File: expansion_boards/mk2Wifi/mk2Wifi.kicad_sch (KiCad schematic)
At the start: 23 parts, among them J0 TRIG_EXT, J2 USB_C_Receptacle_USB2.0_16P, J3 UART_EXT, J4 OLED, SW1 SW_Push, U1 ESP32-C3-MINI-1, U2 AP2112K-3.3

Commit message: Add mk2Wifi documentation, board images, and PCB/schematic updates
Add bilingual README (French default, English translation) with BOM,
connector pinouts, GPIO mapping, power supply details, programming
instructions, and USB-C safety warning. Include trimmed 3D render
images (front, back, SMD, bare board) in assets/ folder.

Co-Authored-By: Claude Opus 4.6 <noreply@anthropic.com>
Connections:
- net UART_RX: now also U1.31 (GPIO21/U0TXD); no longer U1.30 (GPIO20/U0RXD)
- net UART_TX: now also U1.30 (GPIO20/U0RXD); no longer U1.31 (GPIO21/U0TXD)
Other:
- company: (none) -> Mk2PVRouter.com
- title: (none) -> mk2Wifi
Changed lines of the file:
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@@
 	(generator_version "9.0")
 	(paper "A4")
+	(title_block
+		(title "mk2Wifi")
+		(date "2026-02-16")
+		(rev "v1.0")
+		(company "Mk2PVRouter.com")
+	)
 	(rectangle
 		(start 16.51 17.78)
@@
 		)
 	)
-	(text_box "See 4 Boot Configurations"
-		(exclude_from_sim no)
-		(at 25.4 45.72 0)
-		(size 27.94 3.81)
-		(margins 0.9525 0.9525 0.9525 0.9525)
-		(stroke
-			(width 0)
-			(type default)
-		)
-		(fill
-			(type none)
-		)
-		(effects
-			(font
-				(size 1.27 1.27)
-			)
-			(justify left top)
-		)
-	)
 	(junction
 		(at 26.67 102.87)
@@
 	)
 	(junction
+		(at 118.11 31.75)
+		(diameter 0)
+		(color 0 0 0 0)
+	)
+	(junction
 		(at 135.89 34.29)
 		(diameter 0)
@@
 	(wire
 		(pts
-			(xy 220.98 59.69) (xy 242.57 59.69)
+			(xy 220.98 59.69) (xy 241.3 59.69)
 		)
 		(stroke
@@
 	(wire
 		(pts
-			(xy 242.57 64.77) (xy 229.87 64.77)
+			(xy 241.3 64.77) (xy 229.87 64.77)
+		)
+		(stroke
+			(width 0)
+			(type default)
+		)
+	)
+	(wire
+		(pts
+			(xy 220.98 41.91) (xy 241.3 41.91)
 		)
 		(stroke
@@
 	(wire
 		(pts
-			(xy 220.98 74.93) (xy 242.57 74.93)
+			(xy 220.98 74.93) (xy 241.3 74.93)
 		)
 		(stroke
@@
 	(wire
 		(pts
-			(xy 109.22 34.29) (xy 111.76 34.29)
+			(xy 109.22 34.29) (xy 119.38 34.29)
 		)
 		(stroke
@@
 	(wire
 		(pts
-			(xy 72.39 38.1) (xy 74.93 38.1)
+			(xy 118.11 30.48) (xy 118.11 31.75)
 		)
 		(stroke
@@
 	(wire
 		(pts
-			(xy 220.98 41.91) (xy 242.57 41.91)
+			(xy 72.39 38.1) (xy 74.93 38.1)
 		)
 		(stroke
@@
 	(wire
 		(pts
-			(xy 109.22 31.75) (xy 111.76 31.75)
+			(xy 109.22 31.75) (xy 118.11 31.75)
 		)
 		(stroke
@@
 	(wire
 		(pts
-			(xy 242.57 72.39) (xy 229.87 72.39)
+			(xy 241.3 72.39) (xy 229.87 72.39)
 		)
 		(stroke
@@
 	(wire
 		(pts
-			(xy 220.98 62.23) (xy 242.57 62.23)
+			(xy 220.98 62.23) (xy 241.3 62.23)
 		)
 		(stroke
@@
 	(wire
 		(pts
-			(xy 220.98 67.31) (xy 242.57 67.31)
+			(xy 220.98 67.31) (xy 241.3 67.31)
 		)
 		(stroke
@@
 	(wire
 		(pts
-			(xy 220.98 39.37) (xy 242.57 39.37)
+			(xy 48.26 105.41) (xy 45.72 105.41)
 		)
 		(stroke
@@
 	(wire
 		(pts
-			(xy 48.26 105.41) (xy 45.72 105.41)
+			(xy 135.89 34.29) (xy 135.89 36.83)
 		)
 		(stroke
@@
 	(wire
 		(pts
-			(xy 135.89 34.29) (xy 135.89 36.83)
+			(xy 27.94 35.56) (xy 36.83 35.56)
 		)
 		(stroke
@@
 	(wire
 		(pts
-			(xy 27.94 35.56) (xy 36.83 35.56)
+			(xy 118.11 31.75) (xy 119.38 31.75)
 		)
 		(stroke
@@
 	(wire
 		(pts
-			(xy 220.98 69.85) (xy 242.57 69.85)
+			(xy 220.98 69.85) (xy 241.3 69.85)
 		)
 		(stroke
@@
 	(wire
 		(pts
-			(xy 220.98 77.47) (xy 242.57 77.47)
+			(xy 220.98 77.47) (xy 241.3 77.47)
 		)
 		(stroke
@@
 	(wire
 		(pts
-			(xy 229.87 80.01) (xy 242.57 80.01)
+			(xy 229.87 80.01) (xy 241.3 80.01)
 		)
 		(stroke
@@
 	(wire
 		(pts
-			(xy 220.98 46.99) (xy 242.57 46.99)
+			(xy 220.98 46.99) (xy 241.3 46.99)
 		)
 		(stroke
@@
 	(wire
 		(pts
-			(xy 220.98 49.53) (xy 242.57 49.53)
+			(xy 220.98 49.53) (xy 241.3 49.53)
 		)
 		(stroke
@@
 		)
 	)
+	(wire
+		(pts
+			(xy 220.98 39.37) (xy 241.3 39.37)
+		)
+		(stroke
+			(width 0)
+			(type default)
+		)
+	)
 	(label "GPIO9"
-		(at 242.57 77.47 180)
+		(at 241.3 77.47 180)
 		(effects
 			(font
@@
 	)
 	(label "GPIO8"
-		(at 242.57 74.93 180)
+		(at 241.3 74.93 180)
 		(effects
 			(font
@@
 	)
 	(label "D5"
-		(at 242.57 64.77 180)
+		(at 241.3 64.77 180)
 		(effects
 			(font
@@
 	)
 	(label "SDA"
-		(at 242.57 67.31 180)
+		(at 241.3 67.31 180)
 		(effects
 			(font
@@
 	)
 	(label "D9"
-		(at 242.57 72.39 180)
+		(at 241.3 72.39 180)
 		(effects
 			(font
@@
 	)
 	(label "USB_DP"
-		(at 242.57 46.99 180)
+		(at 241.3 46.99 180)
 		(effects
 			(font
@@
 	)
 	(label "SCL"
-		(at 242.57 69.85 180)
+		(at 241.3 69.85 180)
 		(effects
 			(font
@@
 	)
 	(label "D6"
-		(at 242.57 80.01 180)
+		(at 241.3 80.01 180)
 		(effects
 			(font
@@
 	)
 	(label "USB_DN"
-		(at 242.57 49.53 180)
+		(at 241.3 49.53 180)
 		(effects
 			(font
@@
 	)
 	(label "UART_RX"
-		(at 242.57 41.91 180)
+		(at 241.3 39.37 180)
 		(effects
 			(font
@@
 	)
 	(label "GPIO2"
-		(at 242.57 59.69 180)
+		(at 241.3 59.69 180)
 		(effects
 			(font
@@
 	)
 	(label "DS18B20"
-		(at 242.57 62.23 180)
+		(at 241.3 62.23 180)
 		(effects
 			(font
@@
 	)
 	(label "UART_TX"
-		(at 242.57 39.37 180)
+		(at 241.3 41.91 180)
 		(effects
 			(font
@@
 	(symbol
 		(lib_id "power:+3.3V")
-		(at 111.76 31.75 270)
+		(at 119.38 31.75 270)
 		(unit 1)
 		(exclude_from_sim no)
@@
 		(fields_autoplaced yes)
 		(property "Reference" "#PWR6"
-			(at 107.95 31.75 0)
+			(at 115.57 31.75 0)
 			(effects
 				(font
@@
 		)
 		(property "Value" "+3.3V"
-			(at 115.57 31.7499 90)
+			(at 123.19 31.7499 90)
 			(effects
 				(font
@@
 		)
 		(property "Footprint" ""
-			(at 111.76 31.75 0)
+			(at 119.38 31.75 0)
 			(effects
 				(font
@@
 		)
 		(property "Datasheet" ""
-			(at 111.76 31.75 0)
+			(at 119.38 31.75 0)
 			(effects
 				(font
@@
 		)
 		(property "Description" "Power symbol creates a global label with name \"+3.3V\""
-			(at 111.76 31.75 0)
+			(at 119.38 31.75 0)
 			(effects
 				(font
@@
 	(symbol
 		(lib_id "power:PWR_FLAG")
-		(at 109.22 31.75 0)
+		(at 118.11 30.48 0)
 		(unit 1)
 		(exclude_from_sim no)
@@
 		(on_board yes)
 		(dnp no)
+		(fields_autoplaced yes)
 		(property "Reference" "#FLG02"
-			(at 109.22 29.845 0)
+			(at 118.11 28.575 0)
 			(effects
 				(font
@@
 		)
 		(property "Value" "PWR_FLAG"
-			(at 109.22 27.94 0)
+			(at 120.65 29.2099 0)
 			(effects
 				(font
 					(size 1.27 1.27)
 				)
+				(justify left)
 			)
 		)
 		(property "Footprint" ""
-			(at 109.22 31.75 0)
+			(at 118.11 30.48 0)
 			(effects
 				(font
@@
 		)
 		(property "Datasheet" "~"
-			(at 109.22 31.75 0)
+			(at 118.11 30.48 0)
 			(effects
 				(font
@@
 		)
 		(property "Description" "Special symbol for telling ERC where power comes from"
-			(at 109.22 31.75 0)
+			(at 118.11 30.48 0)
 			(effects
 				(font
@@
 	(symbol
 		(lib_id "power:GND")
-		(at 111.76 34.29 90)
+		(at 119.38 34.29 90)
 		(unit 1)
 		(exclude_from_sim no)
@@
 		(fields_autoplaced yes)
 		(property "Reference" "#PWR5"
-			(at 118.11 34.29 0)
+			(at 125.73 34.29 0)
 			(effects
 				(font
@@
 		)
 		(property "Value" "GND"
-			(at 115.57 34.2899 90)
+			(at 123.19 34.2899 90)
 			(effects
 				(font
@@
 		)
 		(property "Footprint" ""
-			(at 111.76 34.29 0)
+			(at 119.38 34.29 0)
 			(effects
 				(font
@@
 		)
 		(property "Datasheet" ""
-			(at 111.76 34.29 0)
+			(at 119.38 34.29 0)
 			(effects
 				(font
@@
 		)
 		(property "Description" "Power symbol creates a global label with name \"GND\" , ground"
-			(at 111.76 34.29 0)
+			(at 119.38 34.29 0)
 			(effects
 				(font

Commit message: Add LCSC part numbers, MPC10-5 footprint, and simulation updates
- Add LCSC fields to mk2Wifi schematic (20 components for JLCPCB assembly)
- Add LCSC fields to mainboard schematic (18x 20K resistors, 12x 100nF caps)
- Add power indicator LED (LED40) and series resistor (R43) to mainboard
- Add MPC10-5 AC-DC converter custom footprint and TMF_05105 3D model
- Add CT and combined bias divider simulation schematics with generators
- Update mainboard PCB layout and bias divider simulation

Co-Authored-By: Claude Opus 4.6 <noreply@anthropic.com>
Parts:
- C1, C4: LCSC (none) -> C1525
- C2, C5: LCSC (none) -> C19666
- D1: LCSC (none) -> C2286
- J2: LCSC (none) -> C2765186
- R1, R3, R4: LCSC (none) -> C25744
- R10, R11, R2, R5, R6, R9: LCSC (none) -> C11702
- R7, R8: LCSC (none) -> C25905
- SW1: LCSC (none) -> C2689642
- U1: LCSC (none) -> C2838502
- U2: LCSC (none) -> C23380830
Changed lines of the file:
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@@
 			)
 		)
+		(property "LCSC" "C11702"
+			(at 160.02 41.91 0)
+			(effects
+				(font
+					(size 1.27 1.27)
+				)
+				(hide yes)
+			)
+		)
 		(pin "1"
 		)
@@
 			)
 		)
+		(property "LCSC" "C11702"
+			(at 226.314 64.77 0)
+			(effects
+				(font
+					(size 1.27 1.27)
+				)
+				(hide yes)
+			)
+		)
 		(pin "1"
 		)
@@
 			)
 		)
+		(property "LCSC" "C1525"
+			(at 62.23 63.4999 0)
+			(effects
+				(font
+					(size 1.27 1.27)
+				)
+				(hide yes)
+			)
+		)
 		(pin "1"
 		)
@@
 			)
 		)
+		(property "LCSC" "C1525"
+			(at 139.7 41.9099 0)
+			(effects
+				(font
+					(size 1.27 1.27)
+				)
+				(hide yes)
+			)
+		)
 		(pin "1"
 		)
@@
 			)
 		)
+		(property "LCSC" "C25744"
+			(at 46.99 63.4999 0)
+			(effects
+				(font
+					(size 1.27 1.27)
+				)
+				(hide yes)
+			)
+		)
 		(pin "1"
 		)
@@
 			)
 		)
+		(property "LCSC" "C2765186"
+			(at 226.06 101.6 0)
+			(effects
+				(font
+					(size 1.27 1.27)
+				)
+				(hide yes)
+			)
+		)
 		(pin "A1"
 		)
@@
 			)
 		)
+		(property "LCSC" "C19666"
+			(at 82.55 110.4899 0)
+			(effects
+				(font
+					(size 1.27 1.27)
+				)
+				(hide yes)
+			)
+		)
 		(pin "1"
 		)
@@
 			)
 		)
+		(property "LCSC" "C2838502"
+			(at 195.1833 29.21 0)
+			(effects
+				(font
+					(size 1.27 1.27)
+				)
+				(hide yes)
+			)
+		)
 		(pin "1"
 		)
@@
 			)
 		)
+		(property "LCSC" "C25905"
+			(at 251.46 138.4299 0)
+			(effects
+				(font
+					(size 1.27 1.27)
+				)
+				(hide yes)
+			)
+		)
 		(pin "1"
 		)
@@
 			)
 		)
+		(property "LCSC" "C25905"
+			(at 262.89 138.4299 0)
+			(effects
+				(font
+					(size 1.27 1.27)
+				)
+				(hide yes)
+			)
+		)
 		(pin "1"
 		)
@@
 			)
 		)
+		(property "LCSC" "C23380830"
+			(at 55.88 99.06 0)
+			(effects
+				(font
+					(size 1.27 1.27)
+				)
+				(hide yes)
+			)
+		)
 		(pin "1"
 		)
@@
 			)
 		)
+		(property "LCSC" "C25744"
+			(at 26.67 63.4999 0)
+			(effects
+				(font
+					(size 1.27 1.27)
+				)
+				(hide yes)
+			)
+		)
 		(pin "1"
 		)
@@
 			)
 		)
+		(property "LCSC" "C2689642"
+			(at 92.71 64.7699 0)
+			(effects
+				(font
+					(size 1.27 1.27)
+				)
+				(hide yes)
+			)
+		)
 		(pin "1"
 		)
@@
 			)
 		)
+		(property "LCSC" "C11702"
+			(at 160.02 39.37 0)
+			(effects
+				(font
+					(size 1.27 1.27)
+				)
+				(hide yes)
+			)
+		)
 		(pin "1"
 		)
@@
 			)
 		)
+		(property "LCSC" "C11702"
+			(at 226.314 72.39 0)
+			(effects
+				(font
+					(size 1.27 1.27)
+				)
+				(hide yes)
+			)
+		)
 		(pin "1"
 		)
@@
 			)
 		)
+		(property "LCSC" "C2286"
+			(at 78.74 75.2474 0)
+			(effects
+				(font
+					(size 1.27 1.27)
+				)
+				(hide yes)
+			)
+		)
 		(pin "1"
 		)
@@
 			)
 		)
+		(property "LCSC" "C19666"
+			(at 30.48 110.4899 0)
+			(effects
+				(font
+					(size 1.27 1.27)
+				)
+				(hide yes)
+			)
+		)
 		(pin "1"
 		)
@@
 			)
 		)
+		(property "LCSC" "C11702"
+			(at 77.47 63.4999 0)
+			(effects
+				(font
+					(size 1.27 1.27)
+				)
+				(hide yes)
+			)
+		)
 		(pin "1"
 		)
@@
 			)
 		)
+		(property "LCSC" "C11702"
+			(at 226.06 80.01 0)
+			(effects
+				(font
+					(size 1.27 1.27)
+				)
+				(hide yes)
+			)
+		)
 		(pin "1"
 		)
@@
 			(effects
 				(font
+					(size 1.27 1.27)
+				)
+				(hide yes)
+			)
+		)
+		(property "LCSC" "C25744"
+			(at 138.43 29.2099 0)
+			(effects
+				(font

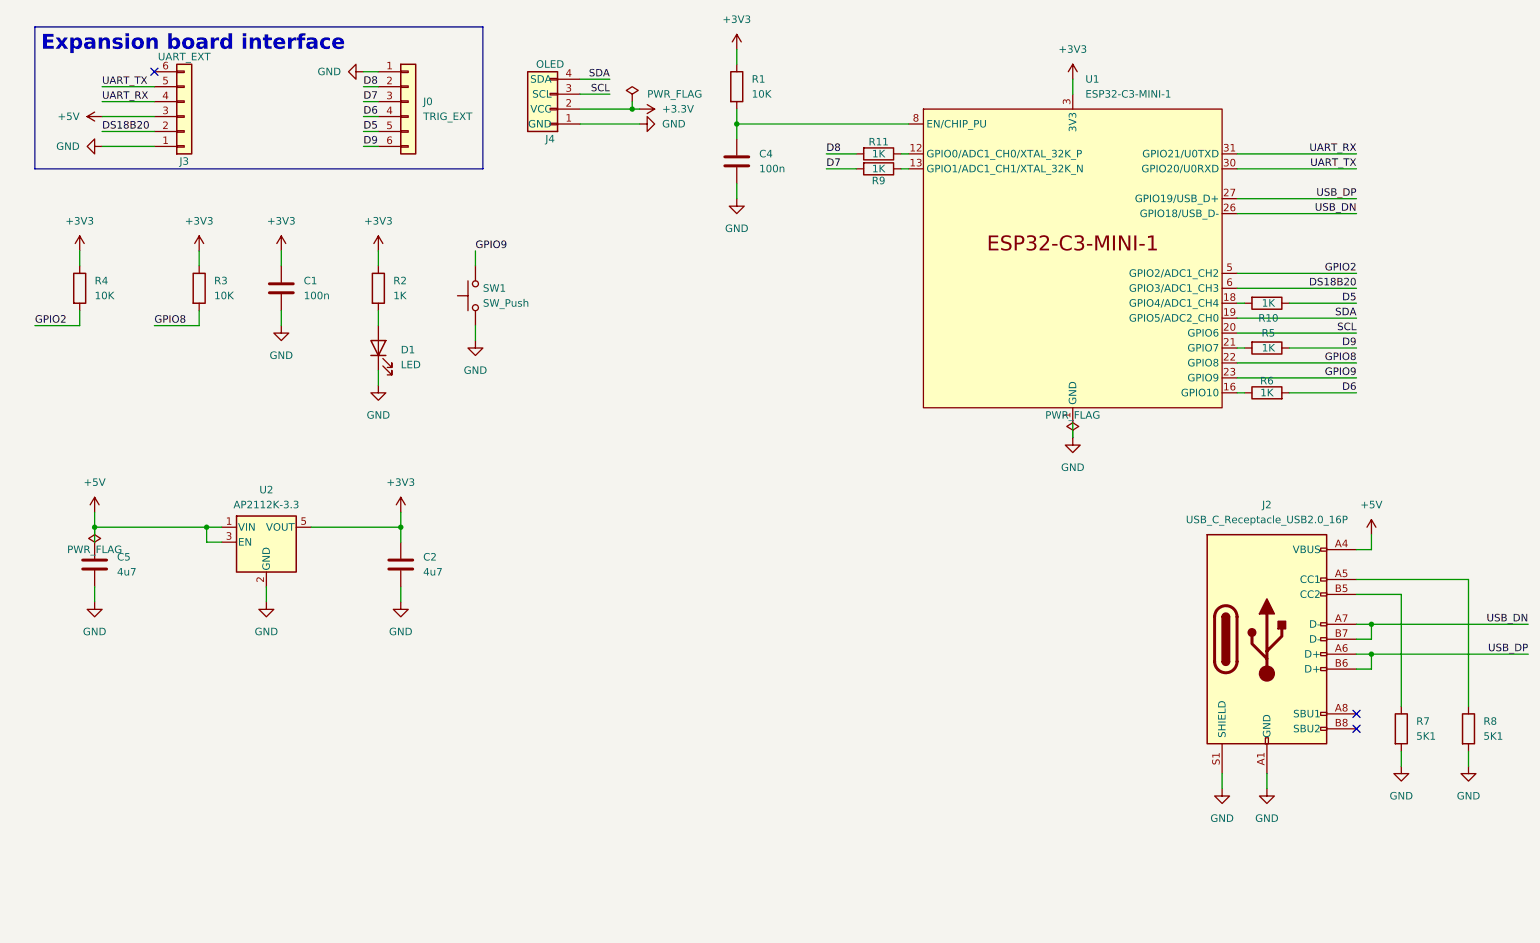
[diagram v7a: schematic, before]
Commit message: Add solder jumpers to mk2Wifi and custom smaller solder jumper footprint
New UserDef footprint: SolderJumper-2_P1.0mm_Open_Pad0.8x1.2mm (compact
1.0mm pitch, 0.8x1.2mm pads, 0.2mm gap for hand soldering).

Co-Authored-By: Claude Opus 4.6 <noreply@anthropic.com>
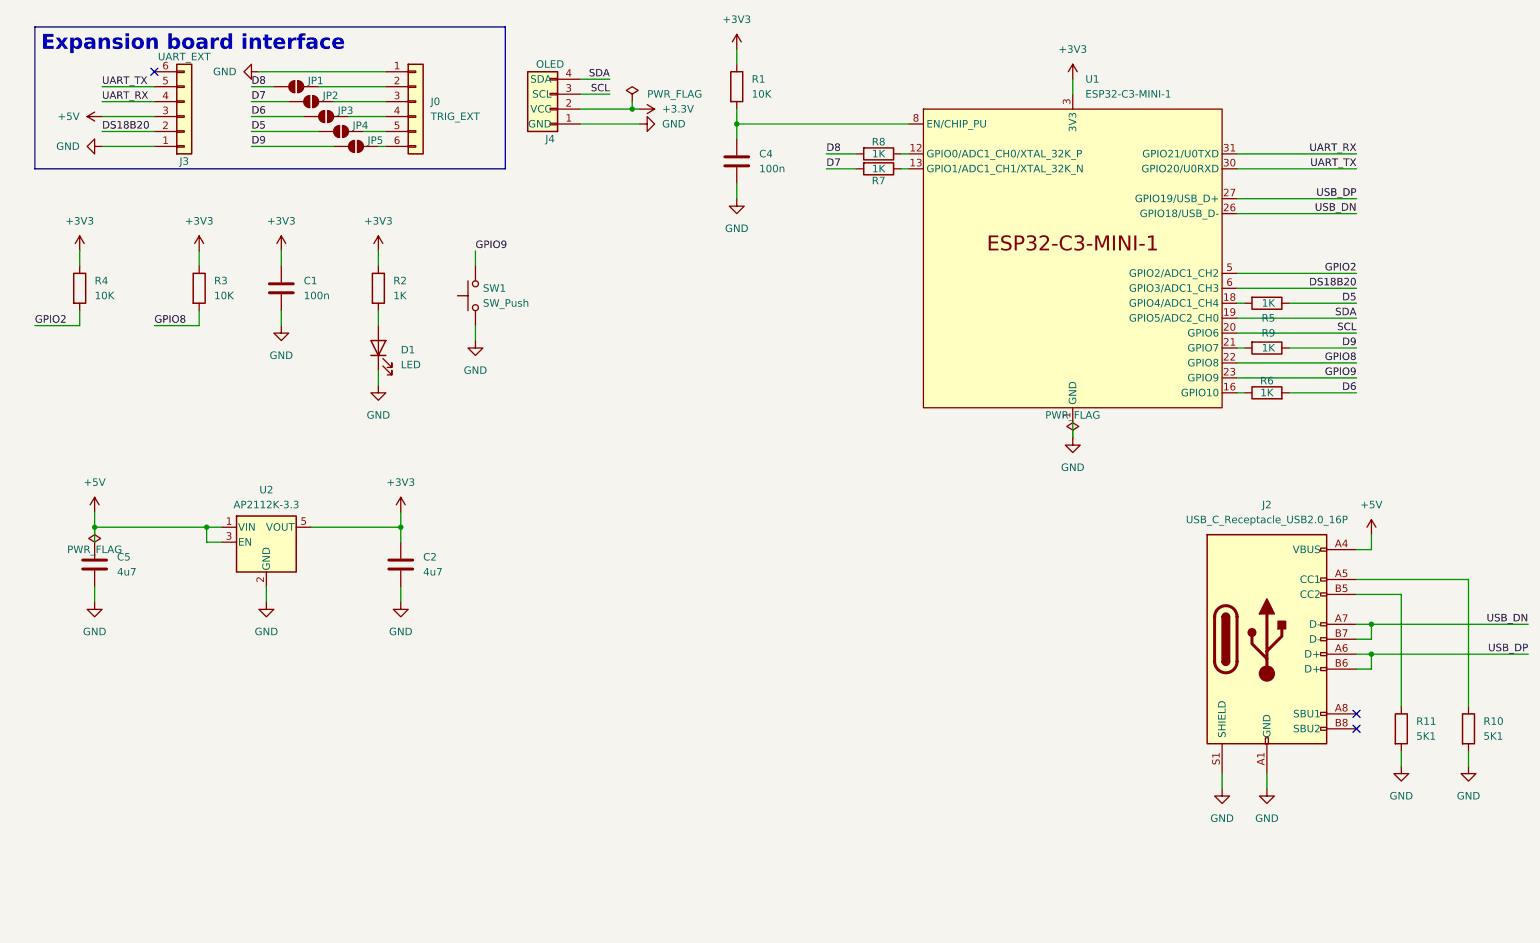
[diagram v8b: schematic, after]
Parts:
- added JP1: D8, UserDef:SolderJumper-2_P1.0mm_Open_Pad0.8x1.2mm, symbol Jumper:SolderJumper_2_Open
- added JP2: D7, UserDef:SolderJumper-2_P1.0mm_Open_Pad0.8x1.2mm, symbol Jumper:SolderJumper_2_Open
- added JP3: D6, UserDef:SolderJumper-2_P1.0mm_Open_Pad0.8x1.2mm, symbol Jumper:SolderJumper_2_Open
- added JP4: D5, UserDef:SolderJumper-2_P1.0mm_Open_Pad0.8x1.2mm, symbol Jumper:SolderJumper_2_Open
- added JP5: D9, UserDef:SolderJumper-2_P1.0mm_Open_Pad0.8x1.2mm, symbol Jumper:SolderJumper_2_Open
- renumbered R8 to R10, R7 to R11, R10 to R5, R9 to R7, R11 to R8, R5 to R9
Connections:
- net D5: now also JP4.1 (A); no longer J0.5 (Pin_5)
- net D6: now also JP3.1 (A); no longer J0.4 (Pin_4)
- net D7: now also JP2.1 (A); no longer J0.3 (Pin_3)
- net D8: now also JP1.1 (A); no longer J0.2 (Pin_2)
- net D9: now also JP5.1 (A); no longer J0.6 (Pin_6)
- new net: J0.2 (Pin_2), JP1.2 (B)
- new net: J0.3 (Pin_3), JP2.2 (B)
- new net: J0.5 (Pin_5), JP4.2 (B)
- new net: J0.4 (Pin_4), JP3.2 (B)
- new net: J0.6 (Pin_6), JP5.2 (B)
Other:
- moved on the sheet: J0
